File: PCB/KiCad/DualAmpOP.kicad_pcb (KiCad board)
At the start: 2 copper layers, 55.9 x 25.4 mm, 21 parts, among them U1 MCP6002

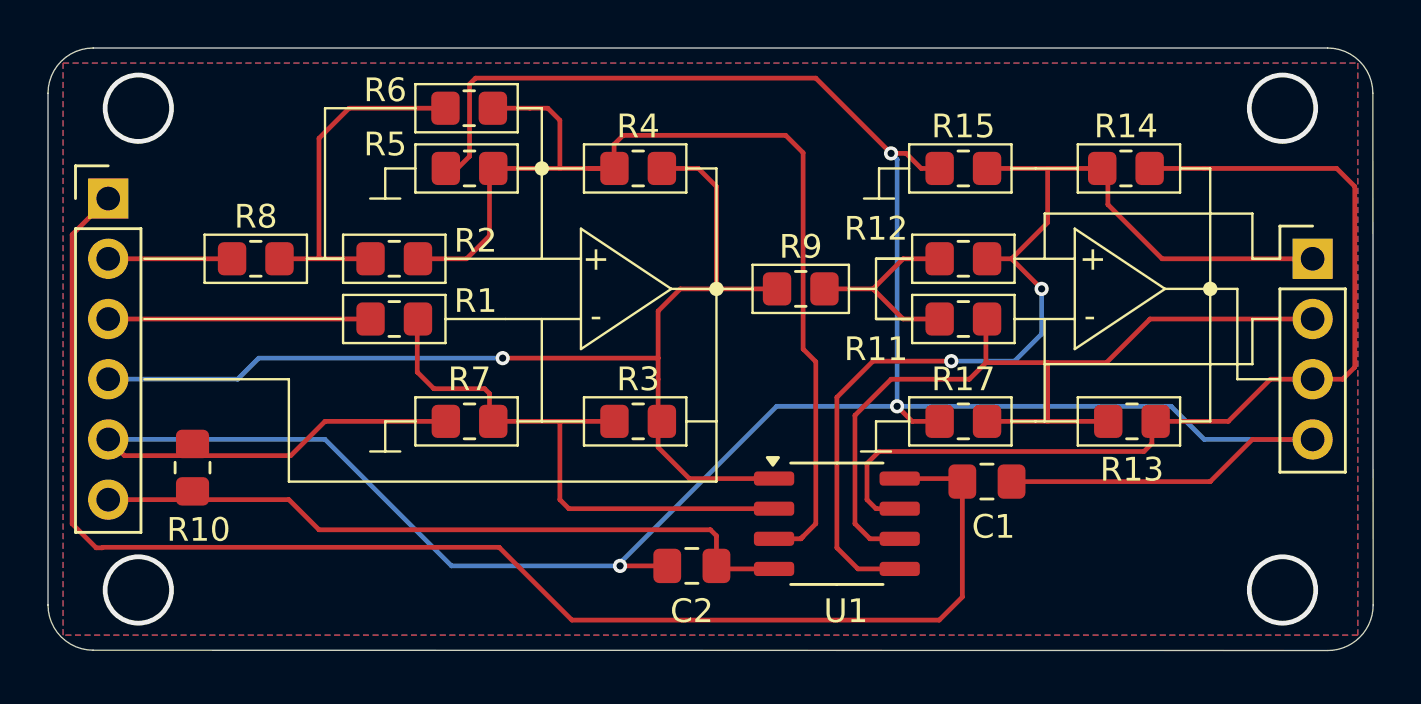
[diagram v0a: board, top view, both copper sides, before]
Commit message: Modification R6 pour filtre Sallen-key
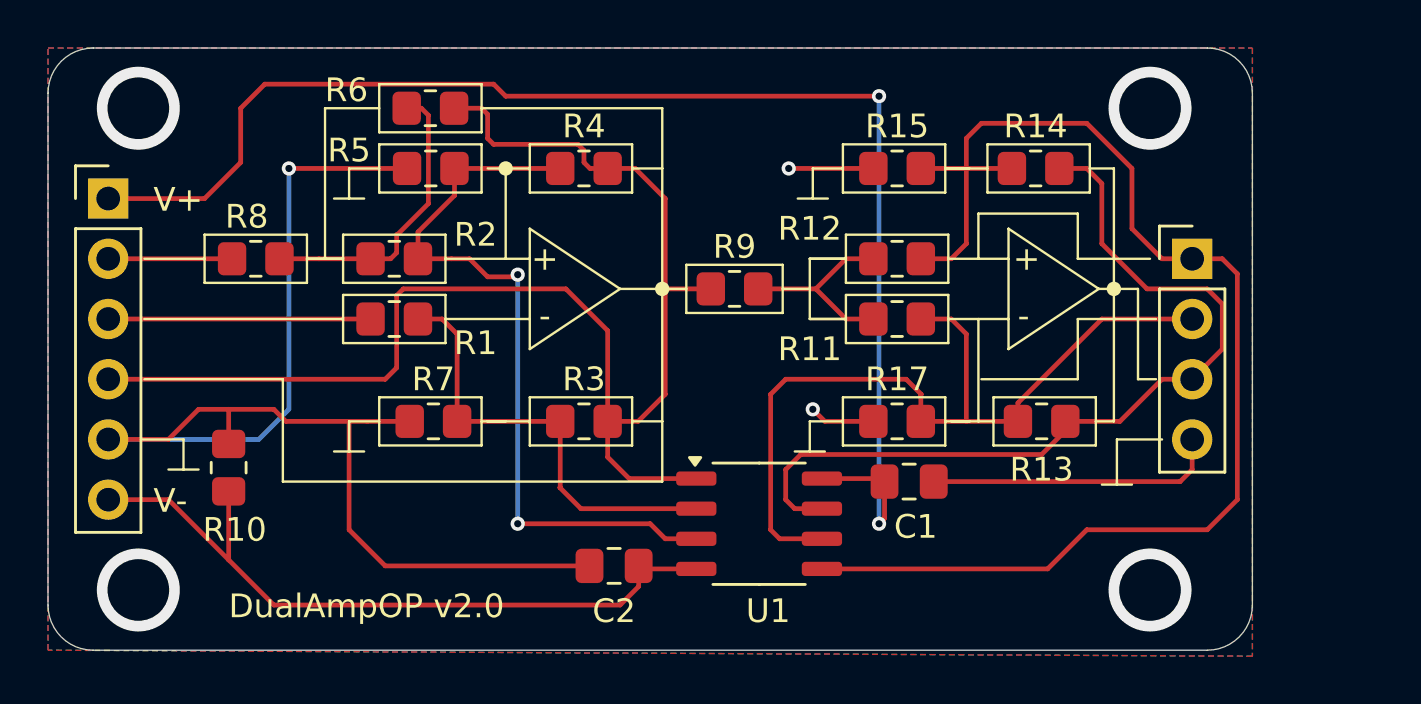
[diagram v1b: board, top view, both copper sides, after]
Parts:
- moved J2 5.08 mm to (147.3, 61.0)
- moved R13 3.81 mm to (141.0, 67.8)
- moved R14 3.81 mm to (140.7, 57.1)
- moved C1 3.28 mm to (135.4, 70.4)
- moved C2 3.28 mm to (122.9, 73.9)
- moved U1 3.28 mm to (129.1, 72.1)
- moved R11 2.79 mm to (134.9, 63.5)
- moved R12 2.79 mm to (134.9, 61.0)
- moved R15 2.79 mm to (134.9, 57.1)
- moved R17 2.79 mm to (134.9, 67.8)
- moved R9 2.79 mm to (128.0, 62.2)
- moved R3 2.29 mm to (121.7, 67.8)
- moved R4 2.29 mm to (121.7, 57.1)
- moved R5 1.64 mm to (115.2, 57.1)
- moved R6 1.64 mm to (115.2, 54.6)
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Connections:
- R6 pad 2: Net-(U1A-+) -> Net-(J1-Pin_4)
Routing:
- net GND: track 126.6 -> 72.1 mm
- net Net-(U1A-+): track 45.3 -> 32.0 mm, vias 0 -> 2
- net Net-(J1-Pin_4): track 47.3 -> 59.1 mm, vias 1 -> 0
- net Net-(J2-Pin_1): track 44.7 -> 54.5 mm, vias 2 -> 0
- net Net-(J2-Pin_3): track 42.4 -> 36.3 mm
- net Net-(U1A--): track 24.6 -> 18.9 mm
- net Net-(J1-Pin_1): track 61.6 -> 58.7 mm, vias 0 -> 2
- net Net-(R2-Pad1): track 14.9 -> 12.5 mm
- net Net-(J2-Pin_2): track 37.4 -> 35.6 mm
- net Net-(J1-Pin_6): track 30.0 -> 30.8 mm
- net Net-(R11-Pad1): track 8.96 -> 8.34 mm
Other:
- board size 55.9 x 25.4 mm -> 50.8 x 25.4 mm
- board text added: "DualAmpOP v2.0"
- board text added: "V+"
- board text added: "V-"
